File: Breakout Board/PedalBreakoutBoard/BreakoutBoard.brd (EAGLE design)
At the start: 69.5 x 63.5 mm, 36 parts

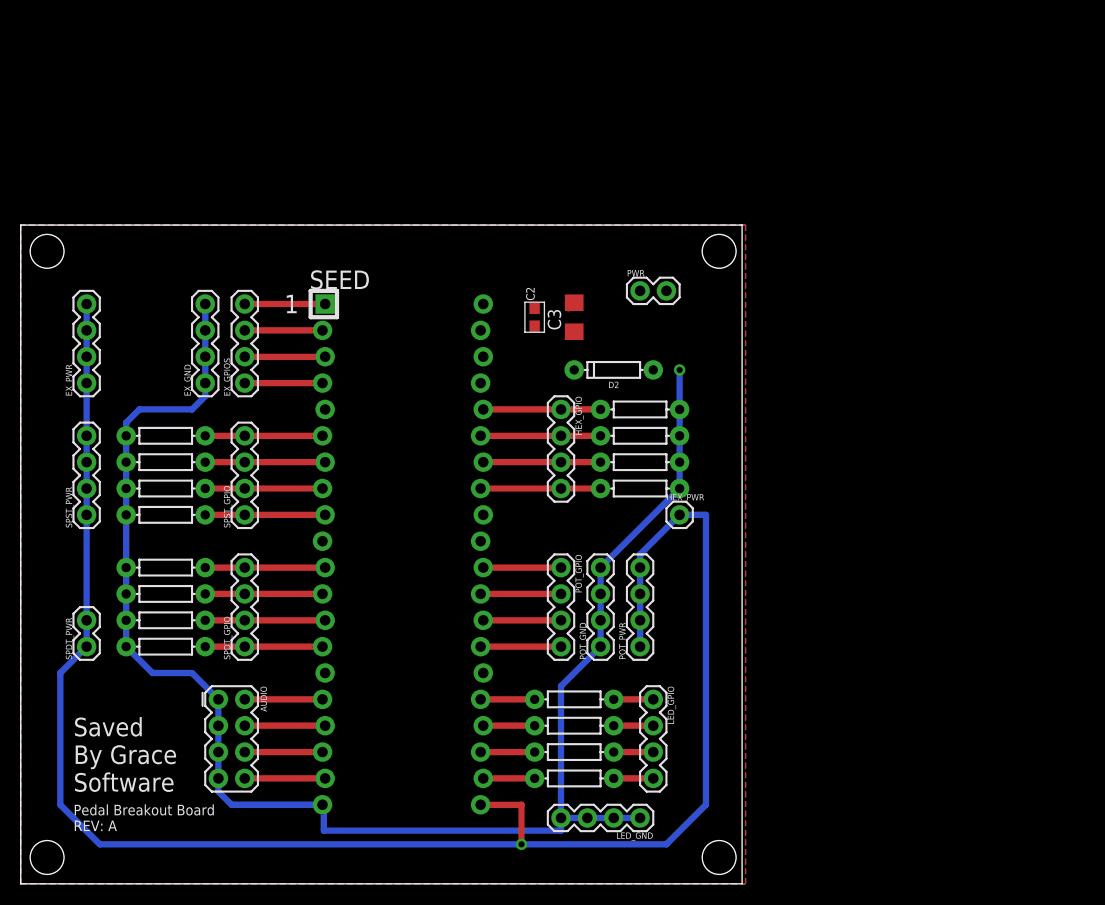
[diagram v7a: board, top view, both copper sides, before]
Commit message: DP-16 - Update capacitors to through hole components
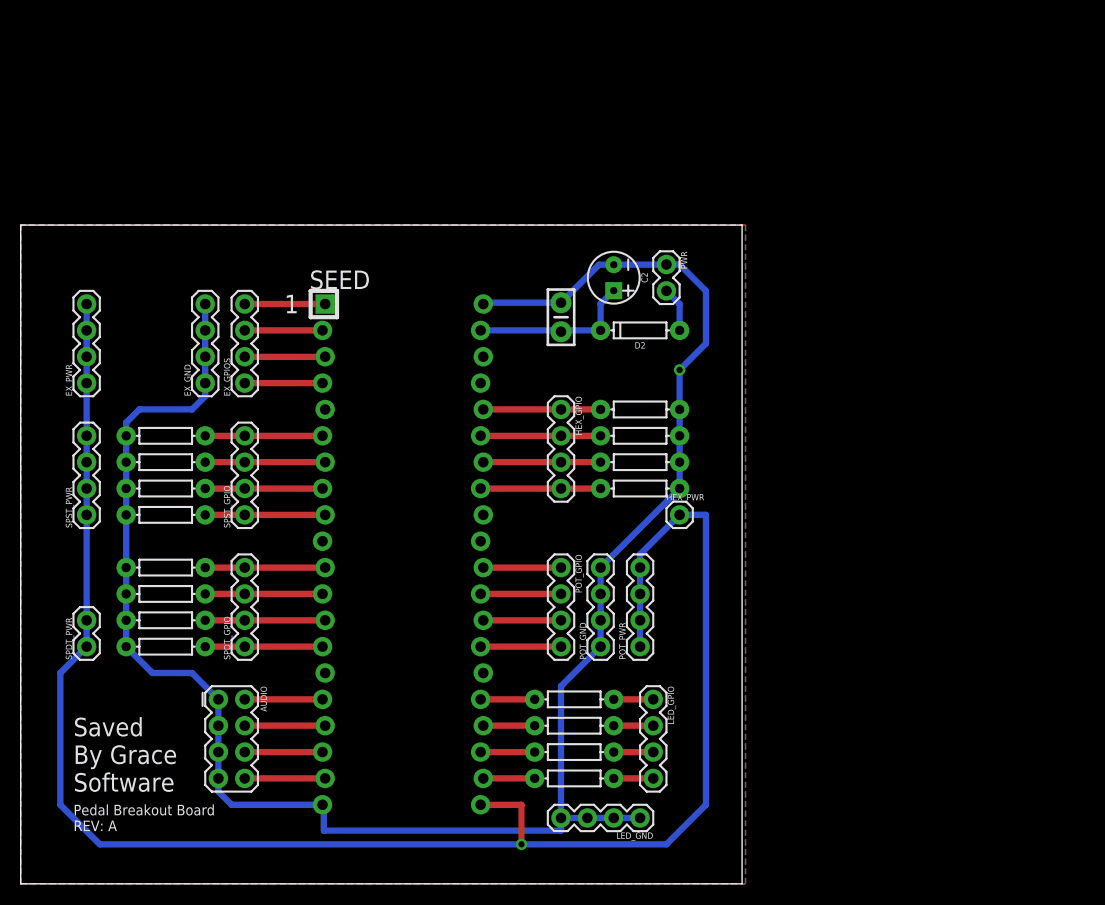
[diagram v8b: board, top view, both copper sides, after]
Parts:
- removed C3: 22UF, Electrosmith-Passives:C1206
- added C1: 0.1uF, SparkFun-Capacitors:CAP-PTH-SMALL-KIT
- C2: value 100NF -> 10uF; device Electrosmith-Passives:C0603 -> SparkFun-Capacitors:CPOL-RADIAL-2.5MM-5MM
- moved C2 8.52 mm to (54.6, 55.9), turned to 270 degrees
- moved D2 4.58 mm to (57.1, 50.8)
- moved PWR 3.59 mm to (59.7, 57.1), turned to 270 degrees
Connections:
- net +9V_IN: now also C1.1; no longer C3.1
- net GND: now also C1.2; no longer C3.2
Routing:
- net GND: track 153.1 -> 184.5 mm
- net +9V_IN: track 0.78 -> 16.0 mm
- net N$2: track 0.00 -> 4.34 mm
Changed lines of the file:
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@@
 By Grace
 Software</text>
-<hole x="0" y="58.42" drill="3.2639"/>
-<hole x="64.77" y="58.42" drill="3.2639"/>
-<hole x="64.77" y="0" drill="3.2639"/>
-<hole x="0" y="0" drill="3.2639"/>
 </plain>
 <attributes>
@@
 </autorouter>
 <elements>
-<element name="C2" library="Electrosmith-Passives" package="C0603" package3d_urn="urn:adsk.eagle:package:23616/2" value="100NF" x="46.99" y="52.07" smashed="yes" rot="R90">
-<attribute name="BIN#" value="" x="132.08" y="96.52" size="1.778" layer="27" rot="R90" display="off"/>
-<attribute name="IPN" value="" x="132.08" y="96.52" size="1.778" layer="27" rot="R90" display="off"/>
-<attribute name="MPN" value="" x="132.08" y="96.52" size="1.778" layer="27" rot="R90" display="off"/>
-<attribute name="NAME" x="46.99" y="53.6575" size="0.8128" layer="25" rot="R90"/>
-<attribute name="PACKAGE" value="C0603" x="132.08" y="96.52" size="1.778" layer="27" rot="R90" display="off"/>
-<attribute name="VALUE" x="47.9425" y="53.6575" size="0.8128" layer="27" rot="R90"/>
-</element>
-<element name="C3" library="Electrosmith-Passives" package="C1206" package3d_urn="urn:adsk.eagle:package:23618/2" value="22UF" x="50.8" y="52.07" smashed="yes" rot="R90">
-<attribute name="BIN#" value="" x="111.76" y="77.47" size="1.778" layer="27" rot="R90" display="off"/>
-<attribute name="IPN" value="" x="111.76" y="77.47" size="1.778" layer="27" rot="R90" display="off"/>
-<attribute name="MPN" value="" x="111.76" y="77.47" size="1.778" layer="27" rot="R90" display="off"/>
-<attribute name="NAME" x="49.53" y="50.8" size="1.27" layer="25" rot="R90"/>
-<attribute name="PACKAGE" value="C1206" x="111.76" y="77.47" size="1.778" layer="27" rot="R90" display="off"/>
-<attribute name="VALUE" x="53.34" y="50.8" size="1.27" layer="27" rot="R90"/>
-</element>
 <element name="L1" library="SparkFun-Resistors" library_urn="urn:adsk.eagle:library:532" package="AXIAL-0.3" package3d_urn="urn:adsk.eagle:package:39658/1" value="330" x="50.8" y="15.24" smashed="yes">
 <attribute name="PROD_ID" value="RES-8371" x="83.82" y="-44.45" size="1.778" layer="27" display="off"/>
@@
 <attribute name="NAME" x="25.29" y="54.785" size="1.778" layer="21"/>
 </element>
-<element name="PWR" library="SparkFun-Connectors" library_urn="urn:adsk.eagle:library:513" package="1X02" package3d_urn="urn:adsk.eagle:package:38039/1" value="" x="57.15" y="54.61" smashed="yes">
-<attribute name="NAME" x="55.88" y="56.007" size="0.6096" layer="25" font="vector" ratio="20"/>
-<attribute name="VALUE" x="55.88" y="52.578" size="0.6096" layer="27" font="vector" ratio="20"/>
+<element name="PWR" library="SparkFun-Connectors" library_urn="urn:adsk.eagle:library:513" package="1X02" package3d_urn="urn:adsk.eagle:package:38039/1" value="" x="59.69" y="57.15" smashed="yes" rot="R270">
+<attribute name="NAME" x="61.087" y="58.42" size="0.6096" layer="25" font="vector" ratio="20" rot="R270"/>
+<attribute name="VALUE" x="57.658" y="58.42" size="0.6096" layer="27" font="vector" ratio="20" rot="R270"/>
 </element>
 <element name="AUDIO" library="SparkFun-Connectors" library_urn="urn:adsk.eagle:library:513" package="2X4" package3d_urn="urn:adsk.eagle:package:38103/1" value="" x="17.78" y="11.43" smashed="yes" rot="R270">
@@
 <attribute name="VALUE" x="17.272" y="44.45" size="0.6096" layer="27" font="vector" ratio="20" rot="R90"/>
 </element>
-<element name="D2" library="SparkFun-DiscreteSemi" library_urn="urn:adsk.eagle:library:514" package="DIODE-1N4148" package3d_urn="urn:adsk.eagle:package:38452/1" value="200mA/100V/1V" x="54.61" y="46.99" smashed="yes" rot="R180">
-<attribute name="NAME" x="54.61" y="45.847" size="0.6096" layer="25" font="vector" ratio="20" rot="R180" align="bottom-center"/>
-<attribute name="PROD_ID" value="DIO-08378" x="54.61" y="46.99" size="1.778" layer="27" rot="R180" display="off"/>
-<attribute name="VALUE" x="54.61" y="48.133" size="0.6096" layer="27" font="vector" ratio="20" rot="R180" align="top-center"/>
+<element name="D2" library="SparkFun-DiscreteSemi" library_urn="urn:adsk.eagle:library:514" package="DIODE-1N4148" package3d_urn="urn:adsk.eagle:package:38452/1" value="200mA/100V/1V" x="57.15" y="50.8" smashed="yes" rot="R180">
+<attribute name="NAME" x="57.15" y="49.657" size="0.6096" layer="25" font="vector" ratio="20" rot="R180" align="bottom-center"/>
+<attribute name="PROD_ID" value="DIO-08378" x="57.15" y="50.8" size="1.778" layer="27" rot="R180" display="off"/>
+<attribute name="VALUE" x="57.15" y="51.943" size="0.6096" layer="27" font="vector" ratio="20" rot="R180" align="top-center"/>
+</element>
+<element name="C1" library="SparkFun-Capacitors" library_urn="urn:adsk.eagle:library:510" package="CAP-PTH-SMALL-KIT" package3d_urn="urn:adsk.eagle:package:37428/1" value="0.1uF" x="49.53" y="52.07" smashed="yes" rot="R90">
+<attribute name="PROD_ID" value="CAP-08370" x="49.53" y="52.07" size="1.778" layer="27" rot="R90" display="off"/>
+</element>
+<element name="C2" library="SparkFun-Capacitors" library_urn="urn:adsk.eagle:library:510" package="CPOL-RADIAL-2.5MM-5MM" package3d_urn="urn:adsk.eagle:package:37423/1" value="10uF" x="54.61" y="55.88" smashed="yes" rot="R270">
+<attribute name="NAME" x="57.277" y="55.88" size="0.6096" layer="25" font="vector" ratio="20" rot="R270" align="bottom-center"/>
+<attribute name="PROD_ID" value="CAP-08440" x="54.61" y="55.88" size="1.778" layer="27" rot="R270" display="off"/>
+<attribute name="VALUE" x="51.943" y="55.88" size="0.6096" layer="27" font="vector" ratio="20" rot="R270" align="top-center"/>
 </element>
 </elements>
 <signals>
 <signal name="GND">
-<contactref element="C2" pad="2"/>
-<contactref element="C3" pad="2"/>
 <contactref element="SEED" pad="40"/>
 <contactref element="SEED" pad="20"/>
@@
 <wire x1="60.96" y1="40.64" x2="60.96" y2="43.18" width="0.6096" layer="16"/>
 <wire x1="60.96" y1="43.18" x2="60.96" y2="46.99" width="0.6096" layer="16"/>
-<via x="60.96" y="46.99" extent="1-16" drill="0.6"/>
-<wire x1="50.8" y1="53.47" x2="50.25" y2="52.92" width="0.6096" layer="1"/>
-<wire x1="42.457" y1="52.92" x2="42.037" y2="53.34" width="0.6096" layer="1"/>
 <polygon width="0.1524" layer="1" isolate="0.3048">
 <vertex x="67.31" y="-2.54"/>
@@
 <vertex x="67.31" y="60.96"/>
 </polygon>
-<wire x1="50.8" y1="53.47" x2="57.15" y2="54.61" width="0" layer="19" extent="1-1"/>
-<wire x1="46.99" y1="52.92" x2="50.25" y2="52.92" width="0" layer="19" extent="1-1"/>
-<wire x1="42.457" y1="52.92" x2="46.99" y2="52.92" width="0" layer="19" extent="1-1"/>
-<wire x1="60.96" y1="46.99" x2="57.15" y2="54.61" width="0" layer="19" extent="1-1"/>
+<contactref element="C1" pad="2"/>
+<contactref element="C2" pad="2"/>
+<wire x1="60.96" y1="46.99" x2="63.5" y2="49.53" width="0.6096" layer="16"/>
+<wire x1="63.5" y1="49.53" x2="63.5" y2="54.61" width="0.6096" layer="16"/>
+<wire x1="63.5" y1="54.61" x2="60.96" y2="57.15" width="0.6096" layer="16"/>
+<wire x1="60.96" y1="57.15" x2="59.69" y2="57.15" width="0.6096" layer="16"/>
+<wire x1="59.69" y1="57.15" x2="59.67" y2="57.13" width="0.6096" layer="16"/>
+<wire x1="59.67" y1="57.13" x2="54.61" y2="57.13" width="0.6096" layer="16"/>
+<wire x1="54.61" y1="57.13" x2="53.193" y2="57.13" width="0.6096" layer="16"/>
+<wire x1="53.193" y1="57.13" x2="49.53" y2="53.467" width="0.6096" layer="16"/>
+<wire x1="49.53" y1="53.467" x2="42.164" y2="53.467" width="0.6096" layer="16"/>
+<wire x1="42.164" y1="53.467" x2="42.037" y2="53.34" width="0.6096" layer="16"/>
+<via x="60.96" y="46.99" extent="1-16" drill="0.6"/>
 </signal>
 <signal name="SPST1">
@@
 <contactref element="PWR" pad="2"/>
 <contactref element="D2" pad="A"/>
-<wire x1="58.42" y1="46.99" x2="59.69" y2="54.61" width="0" layer="19" extent="1-1"/>
+<wire x1="60.96" y1="50.8" x2="60.96" y2="53.34" width="0.6096" layer="16"/>
+<wire x1="60.96" y1="53.34" x2="59.69" y2="54.61" width="0.6096" layer="16"/>
 </signal>
 <signal name="+9V_IN">
 <contactref element="SEED" pad="39"/>
+<contactref element="D2" pad="C"/>
+<contactref element="C1" pad="1"/>
 <contactref element="C2" pad="1"/>
-<contactref element="C3" pad="1"/>
-<wire x1="50.8" y1="50.67" x2="50.93" y2="50.8" width="0.6096" layer="1"/>
-<wire x1="41.783" y1="50.8" x2="42.203" y2="51.22" width="0.6096" layer="1"/>
-<contactref element="D2" pad="C"/>
-<wire x1="50.8" y1="46.99" x2="50.8" y2="50.67" width="0" layer="19" extent="1-1"/>
-<wire x1="46.99" y1="51.22" x2="50.8" y2="50.67" width="0" layer="19" extent="1-1"/>
-<wire x1="42.203" y1="51.22" x2="46.99" y2="51.22" width="0" layer="19" extent="1-1"/>
+<wire x1="41.783" y1="50.8" x2="49.403" y2="50.8" width="0.6096" layer="16"/>
+<wire x1="49.403" y1="50.8" x2="49.53" y2="50.673" width="0.6096" layer="16"/>
+<wire x1="49.53" y1="50.673" x2="49.657" y2="50.8" width="0.6096" layer="16"/>
+<wire x1="49.657" y1="50.8" x2="53.34" y2="50.8" width="0.6096" layer="16"/>
+<wire x1="53.34" y1="50.8" x2="53.34" y2="53.36" width="0.6096" layer="16"/>
+<wire x1="53.34" y1="53.36" x2="54.61" y2="54.63" width="0.6096" layer="16"/>
 </signal>
 <signal name="N$1">
